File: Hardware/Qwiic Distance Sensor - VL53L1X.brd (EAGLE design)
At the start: 25.4 x 25.4 mm, 46 parts, among them J2 SMD, J3 PTH, J4 SMD, U2 VL53L1X

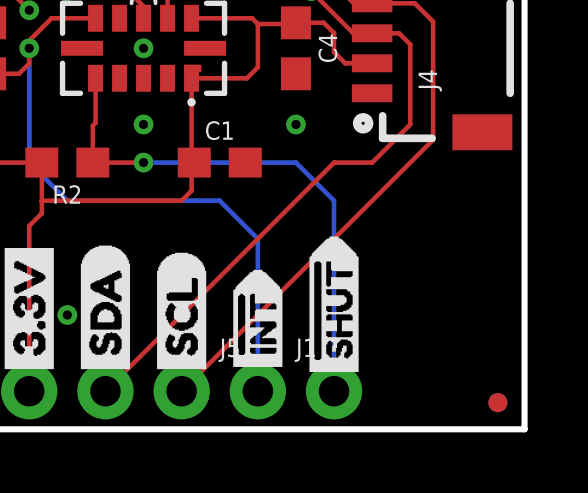
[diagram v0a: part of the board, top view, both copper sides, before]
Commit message: updated silk
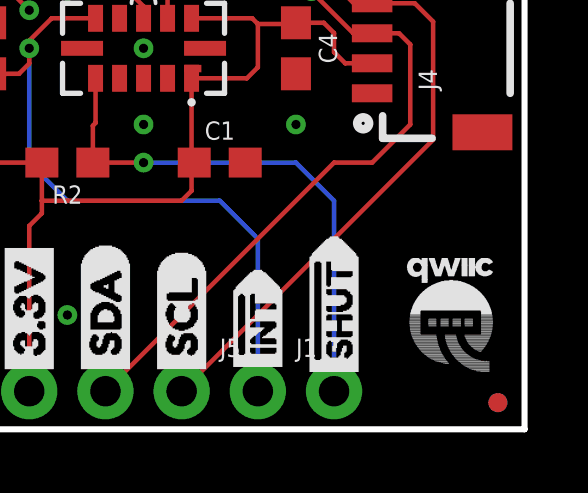
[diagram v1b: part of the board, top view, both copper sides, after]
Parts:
- added U$13: (no value), Labels:QWIIC-LOGO-SMALL
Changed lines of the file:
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@@
 <layer number="59" name="tCarbon" color="7" fill="1" visible="no" active="no"/>
 <layer number="60" name="bCarbon" color="7" fill="1" visible="no" active="no"/>
+<layer number="88" name="SimResults" color="7" fill="1" visible="yes" active="yes"/>
+<layer number="89" name="SimProbes" color="7" fill="1" visible="yes" active="yes"/>
 <layer number="90" name="Modules" color="5" fill="1" visible="no" active="no"/>
 <layer number="97" name="Info" color="7" fill="1" visible="no" active="no"/>
@@
 <element name="U$12" library="Labels-0_04" package="(INT)" value="" x="5.969" y="8.382" rot="MR0"/>
 <element name="LOGO2" library="SparkFun-Aesthetics" package="REVISION" value="REVISION" x="-3.81" y="-11.43"/>
+<element name="U$13" library="Labels" package="QWIIC-LOGO-SMALL" value="" x="22.86" y="3.81"/>
 </elements>
 <signals>

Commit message: updating Qwiic connectors
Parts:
- J2, J4: value SMD -> (none); device SparkX:1X04_1MM_RA -> SparkFun-Connectors:1X04_1MM_RA
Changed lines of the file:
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@@
 </element>
 <element name="I2C" library="SparkFun-Jumpers" package="SMT-JUMPER_3_2-NC_TRACE_SILK" value="" x="12.7" y="16.51" rot="MR0"/>
-<element name="J2" library="SparkX" package="1X04_1MM_RA" value="SMD" x="5.08" y="12.7" rot="R270"/>
+<element name="J2" library="SparkFun-Connectors" package="1X04_1MM_RA" value="" x="5.08" y="12.7" rot="R270">
+<attribute name="PROD_ID" value="CONN-13694" x="5.08" y="12.7" size="1.778" layer="27" rot="R270" display="off"/>
+<attribute name="VALUE" value="" x="5.08" y="12.7" size="1.778" layer="27" rot="R270" display="off"/>
+</element>
 <element name="J3" library="SparkX" package="1X04_NO_SILK" value="PTH" x="6.35" y="1.27"/>
 <element name="FRAME1" library="SparkFun-Aesthetics" package="CREATIVE_COMMONS" value="FRAME-LETTER" x="-15.24" y="-8.89"/>
@@
 <attribute name="VALUE" x="17.018" y="12.7" size="0.6096" layer="27" font="vector" ratio="20" rot="R270" align="top-center"/>
 </element>
-<element name="J4" library="SparkX" package="1X04_1MM_RA" value="SMD" x="20.32" y="12.7" rot="R90"/>
+<element name="J4" library="SparkFun-Connectors" package="1X04_1MM_RA" value="" x="20.32" y="12.7" rot="R90">
+<attribute name="PROD_ID" value="CONN-13694" x="20.32" y="12.7" size="1.778" layer="27" rot="R90" display="off"/>
+<attribute name="VALUE" value="" x="20.32" y="12.7" size="1.778" layer="27" rot="R90" display="off"/>
+</element>
 <element name="LOGO1" library="SparkFun-Aesthetics" package="OSHW-LOGO-MINI" value="OSHW-LOGOMINI" x="2.54" y="3.81" rot="MR0"/>
 <element name="U$1" library="SparkFun-Aesthetics" package="SFE_LOGO_NAME_.1" value="SFE_LOGO_NAME.1_INCH" x="6.604" y="21.59"/>

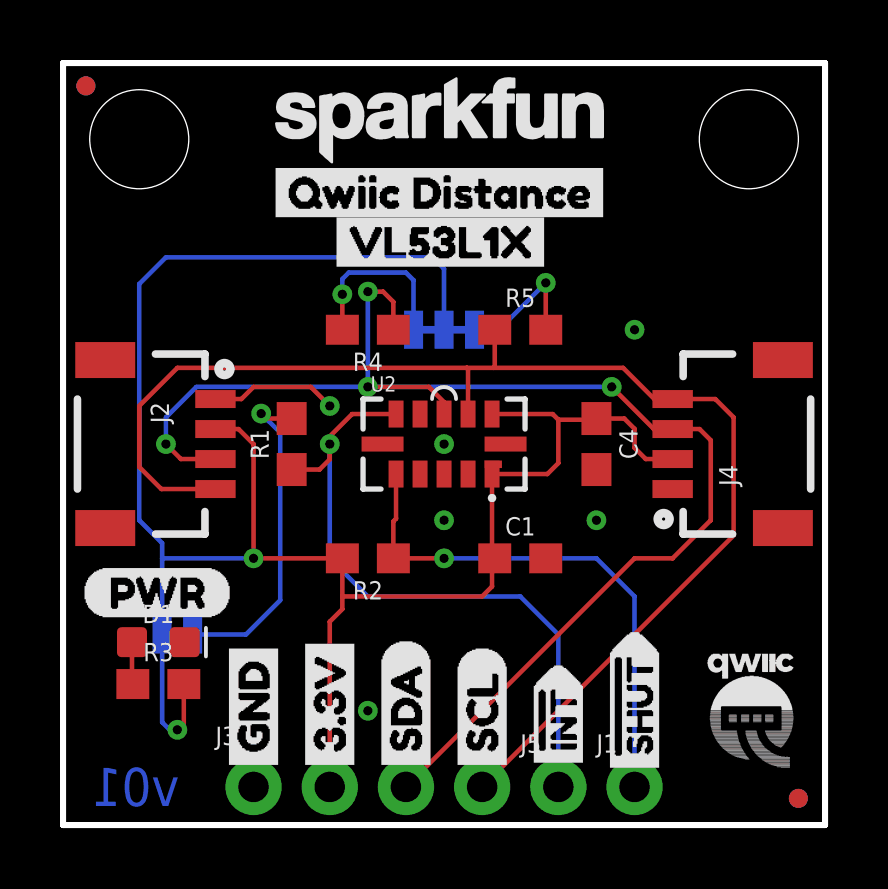
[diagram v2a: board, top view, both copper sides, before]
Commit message: changing INT silk
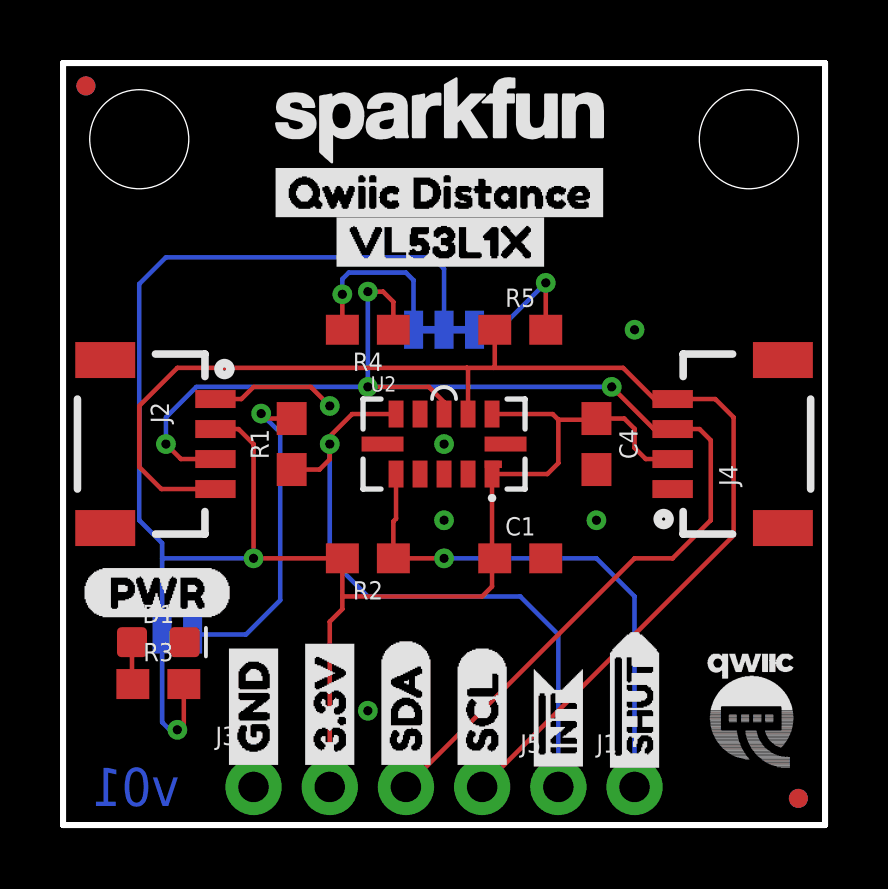
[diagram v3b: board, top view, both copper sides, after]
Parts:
- removed U$25: (no value), Labels-0_04:#INT14
- added U$14: (no value), Labels:INT#-[<
- U$7: device Labels-0_04:#INT14 -> Labels:INT#-[<
- moved U$7 0.13 mm to (16.5, 1.27), flipped to the top
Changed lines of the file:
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@@
 <layer number="22" name="bPlace" color="14" fill="1" visible="yes" active="yes"/>
 <layer number="23" name="tOrigins" color="15" fill="1" visible="yes" active="yes"/>
-<layer number="24" name="bOrigins" color="15" fill="1" visible="no" active="yes"/>
+<layer number="24" name="bOrigins" color="15" fill="1" visible="yes" active="yes"/>
 <layer number="25" name="tNames" color="7" fill="1" visible="yes" active="yes"/>
 <layer number="26" name="bNames" color="7" fill="1" visible="no" active="yes"/>
@@
 <element name="U$21" library="Labels-0_04" package="3#3V2" value="" x="8.89" y="1.524" rot="R90"/>
 <element name="U$22" library="Labels-0_04" package="GND1" value="" x="6.35" y="1.524" rot="R90"/>
-<element name="U$25" library="Labels-0_04" package="#INT14" value="" x="16.51" y="1.397" rot="R90"/>
 <element name="U$26" library="Labels-0_04" package="SCL9" value="" x="13.97" y="1.524" rot="R90"/>
 <element name="U$27" library="Labels-0_04" package="SDA8" value="" x="11.43" y="1.524" rot="R90"/>
@@
 <element name="U$5" library="Labels-0_04" package="SDA8" value="" x="11.43" y="1.524" rot="MR90"/>
 <element name="U$6" library="Labels-0_04" package="SCL9" value="" x="13.97" y="1.524" rot="MR90"/>
-<element name="U$7" library="Labels-0_04" package="#INT14" value="" x="16.51" y="1.397" rot="MR90"/>
 <element name="U$8" library="buzzard_labels (16)" package="#SHUT15" value="" x="19.05" y="1.27" rot="R90"/>
 <element name="U$9" library="buzzard_labels (16)" package="#SHUT15" value="" x="19.05" y="1.27" rot="MR90"/>
@@
 <element name="LOGO2" library="SparkFun-Aesthetics" package="REVISION" value="REVISION" x="-3.81" y="-11.43"/>
 <element name="U$13" library="Labels" package="QWIIC-LOGO-SMALL" value="" x="22.86" y="3.81"/>
+<element name="U$7" library="Labels" package="INT#-[&lt;" value="" x="16.51" y="1.27" rot="R90"/>
+<element name="U$14" library="Labels" package="INT#-[&lt;" value="" x="16.51" y="1.27" rot="MR90"/>
 </elements>
 <signals>
